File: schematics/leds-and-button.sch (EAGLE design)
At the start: 13 parts, among them IC1 74LS595N

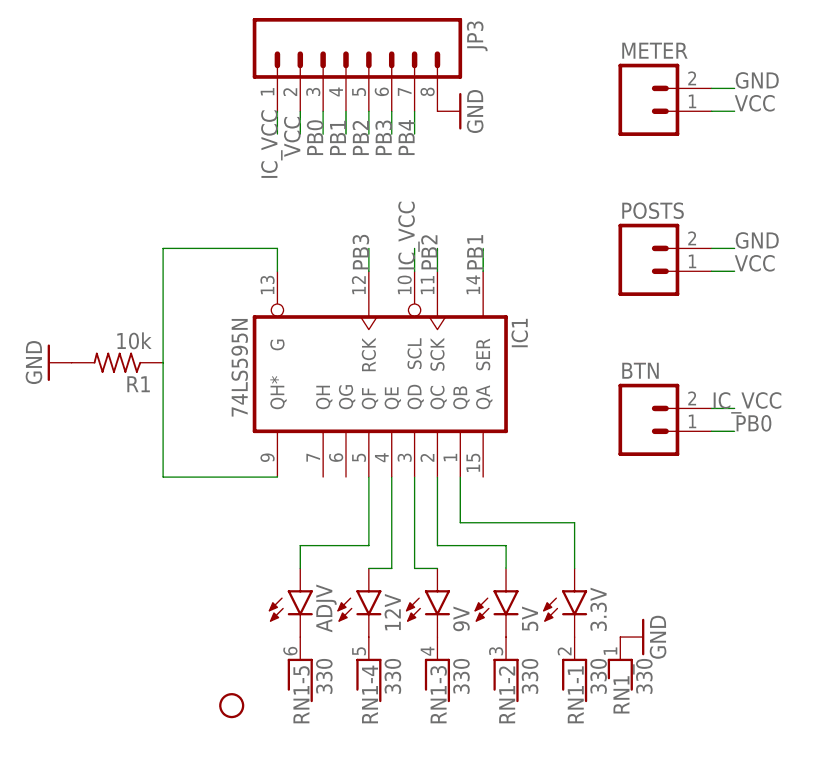
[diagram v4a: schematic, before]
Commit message: Decided to remove the "adjustable" option because it was kinda useless
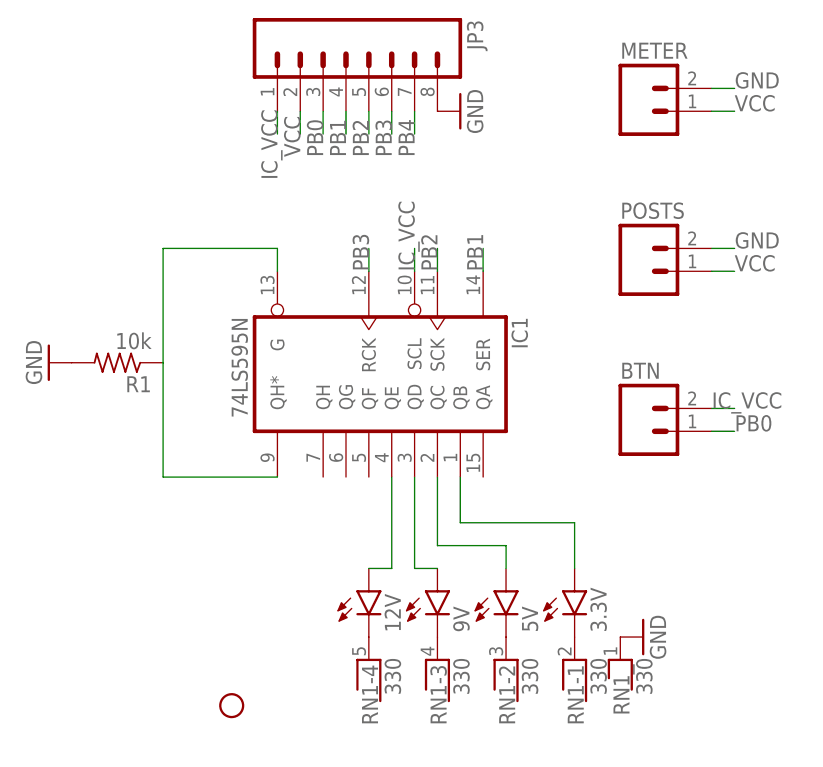
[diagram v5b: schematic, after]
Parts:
- removed ADJV: (no value), SparkFun-LED:LED3MM
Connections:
- removed net N$1: ADJV.C, RN1-5.1
- removed net N$4: ADJV.A, IC1A.QF
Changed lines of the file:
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@@
 <part name="POSTS" library="SparkFun" deviceset="M02" device="PTH"/>
 <part name="METER" library="SparkFun" deviceset="M02" device="PTH"/>
-<part name="ADJV" library="SparkFun-LED" deviceset="LED" device="3MM"/>
 <part name="12V" library="SparkFun-LED" deviceset="LED" device="3MM"/>
 <part name="9V" library="SparkFun-LED" deviceset="LED" device="3MM"/>
@@
 <instance part="RN1" gate="-3" x="43.18" y="10.16" rot="R270"/>
 <instance part="RN1" gate="-4" x="35.56" y="10.16" rot="R270"/>
-<instance part="RN1" gate="-5" x="27.94" y="10.16" rot="R270"/>
 <instance part="JP2" gate="G$1" x="20.32" y="5.08"/>
 <instance part="BTN" gate="G$1" x="66.04" y="35.56"/>
@@
 <instance part="POSTS" gate="G$1" x="66.04" y="53.34"/>
 <instance part="METER" gate="G$1" x="66.04" y="71.12"/>
-<instance part="ADJV" gate="G$1" x="27.94" y="17.78"/>
 <instance part="12V" gate="G$1" x="35.56" y="17.78"/>
 <instance part="9V" gate="G$1" x="43.18" y="17.78"/>
@@
 </busses>
 <nets>
-<net name="N$4" class="0">
-<segment>
-<wire x1="27.94" y1="22.86" x2="27.94" y2="20.32" width="0.1524" layer="91"/>
-<wire x1="35.56" y1="22.86" x2="27.94" y2="22.86" width="0.1524" layer="91"/>
-<pinref part="IC1" gate="A" pin="QF"/>
-<wire x1="35.56" y1="22.86" x2="35.56" y2="30.48" width="0.1524" layer="91"/>
-<pinref part="ADJV" gate="G$1" pin="A"/>
-</segment>
-</net>
 <net name="N$5" class="0">
 <segment>
@@
 </segment>
 </net>
-<net name="N$1" class="0">
-<segment>
-<pinref part="RN1" gate="-5" pin="1"/>
-<pinref part="ADJV" gate="G$1" pin="C"/>
-</segment>
-</net>

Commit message: Tweak tweak
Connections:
- net IC_VCC renamed VIC
- net VCC renamed VADJ
- removed net PB4: JP3.7
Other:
- moved on the sheet: R1
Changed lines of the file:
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@@
 <instance part="GND1" gate="1" x="45.72" y="71.12" rot="R90"/>
 <instance part="GND2" gate="1" x="66.04" y="12.7" rot="R90"/>
-<instance part="GND3" gate="1" x="0" y="43.18" rot="R270"/>
-<instance part="R1" gate="G$1" x="7.62" y="43.18" rot="R180"/>
+<instance part="GND3" gate="1" x="5.08" y="43.18" rot="R270"/>
+<instance part="R1" gate="G$1" x="12.7" y="43.18" rot="R180"/>
 <instance part="POSTS" gate="G$1" x="66.04" y="53.34"/>
 <instance part="METER" gate="G$1" x="66.04" y="71.12"/>
@@
 </segment>
 </net>
-<net name="IC_VCC" class="0">
+<net name="VIC" class="0">
 <segment>
 <pinref part="JP3" gate="G$1" pin="1"/>
 <wire x1="25.4" y1="71.12" x2="25.4" y2="68.58" width="0.1524" layer="91"/>
-<label x="25.4" y="63.5" size="1.778" layer="95" rot="R90"/>
+<label x="25.4" y="66.04" size="1.778" layer="95" rot="R90"/>
 </segment>
 <segment>
 <pinref part="BTN" gate="G$1" pin="2"/>
 <wire x1="73.66" y1="38.1" x2="76.2" y2="38.1" width="0.1524" layer="91"/>
-<label x="73.66" y="38.1" size="1.778" layer="95"/>
+<label x="76.2" y="38.1" size="1.778" layer="95"/>
 </segment>
 <segment>
@@
 <pinref part="IC1" gate="A" pin="QH*"/>
 <pinref part="R1" gate="G$1" pin="1"/>
-<wire x1="25.4" y1="30.48" x2="12.7" y2="30.48" width="0.1524" layer="91"/>
-<wire x1="12.7" y1="30.48" x2="12.7" y2="43.18" width="0.1524" layer="91"/>
-<wire x1="12.7" y1="43.18" x2="12.7" y2="55.88" width="0.1524" layer="91"/>
+<wire x1="25.4" y1="30.48" x2="17.78" y2="30.48" width="0.1524" layer="91"/>
+<wire x1="17.78" y1="30.48" x2="17.78" y2="43.18" width="0.1524" layer="91"/>
+<wire x1="17.78" y1="43.18" x2="17.78" y2="53.34" width="0.1524" layer="91"/>
 <pinref part="IC1" gate="A" pin="G"/>
-<wire x1="12.7" y1="55.88" x2="25.4" y2="55.88" width="0.1524" layer="91"/>
-<wire x1="25.4" y1="55.88" x2="25.4" y2="53.34" width="0.1524" layer="91"/>
+<wire x1="17.78" y1="53.34" x2="25.4" y2="53.34" width="0.1524" layer="91"/>
 </segment>
 </net>
@@
 </segment>
 </net>
-<net name="PB4" class="0">
-<segment>
-<pinref part="JP3" gate="G$1" pin="7"/>
-<wire x1="40.64" y1="71.12" x2="40.64" y2="68.58" width="0.1524" layer="91"/>
-<label x="40.64" y="66.04" size="1.778" layer="95" rot="R90"/>
-</segment>
-</net>
 <net name="PB2" class="0">
 <segment>
@@
 </segment>
 </net>
-<net name="VCC" class="0">
+<net name="VADJ" class="0">
 <segment>
 <pinref part="JP3" gate="G$1" pin="2"/>
